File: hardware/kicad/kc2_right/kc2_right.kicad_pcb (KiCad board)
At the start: 2 copper layers, 193.3 x 132.2 mm, 102 parts, among them SW1 KEY_01, SW10 KEY_10, SW11 KEY_11, SW12 KEY_12, SW13 KEY_13, SW14 KEY_14, SW15 KEY_15, SW16 KEY_16, SW17 KEY_17, SW18 KEY_18, SW19 KEY_19, SW2 KEY_02, SW20 KEY_20, SW21 KEY_21, SW22 KEY_22, SW23 KEY_23, SW24 KEY_24, SW25 KEY_25, SW26 KEY_26, SW27 KEY_27, SW28 KEY_28, SW29 KEY_29, SW3 KEY_03, SW30 KEY_30, SW31 KEY_31, SW32 KEY_32, SW33 KEY_33, SW34 KEY_34, SW35 KEY_35, SW36 KEY_36, SW37 KEY_37, SW38 KEY_38, SW39 KEY_39, SW4 KEY_04, SW40 KEY_40, SW41 KEY_41, SW42 KEY_42, SW43 KEY_43, SW44 KEY_44, SW45 KEY_45, SW5 KEY_05, SW6 KEY_06, SW7 KEY_07, SW8 KEY_08, SW9 KEY_09, U1 nice!nano_v2_socket_24pin

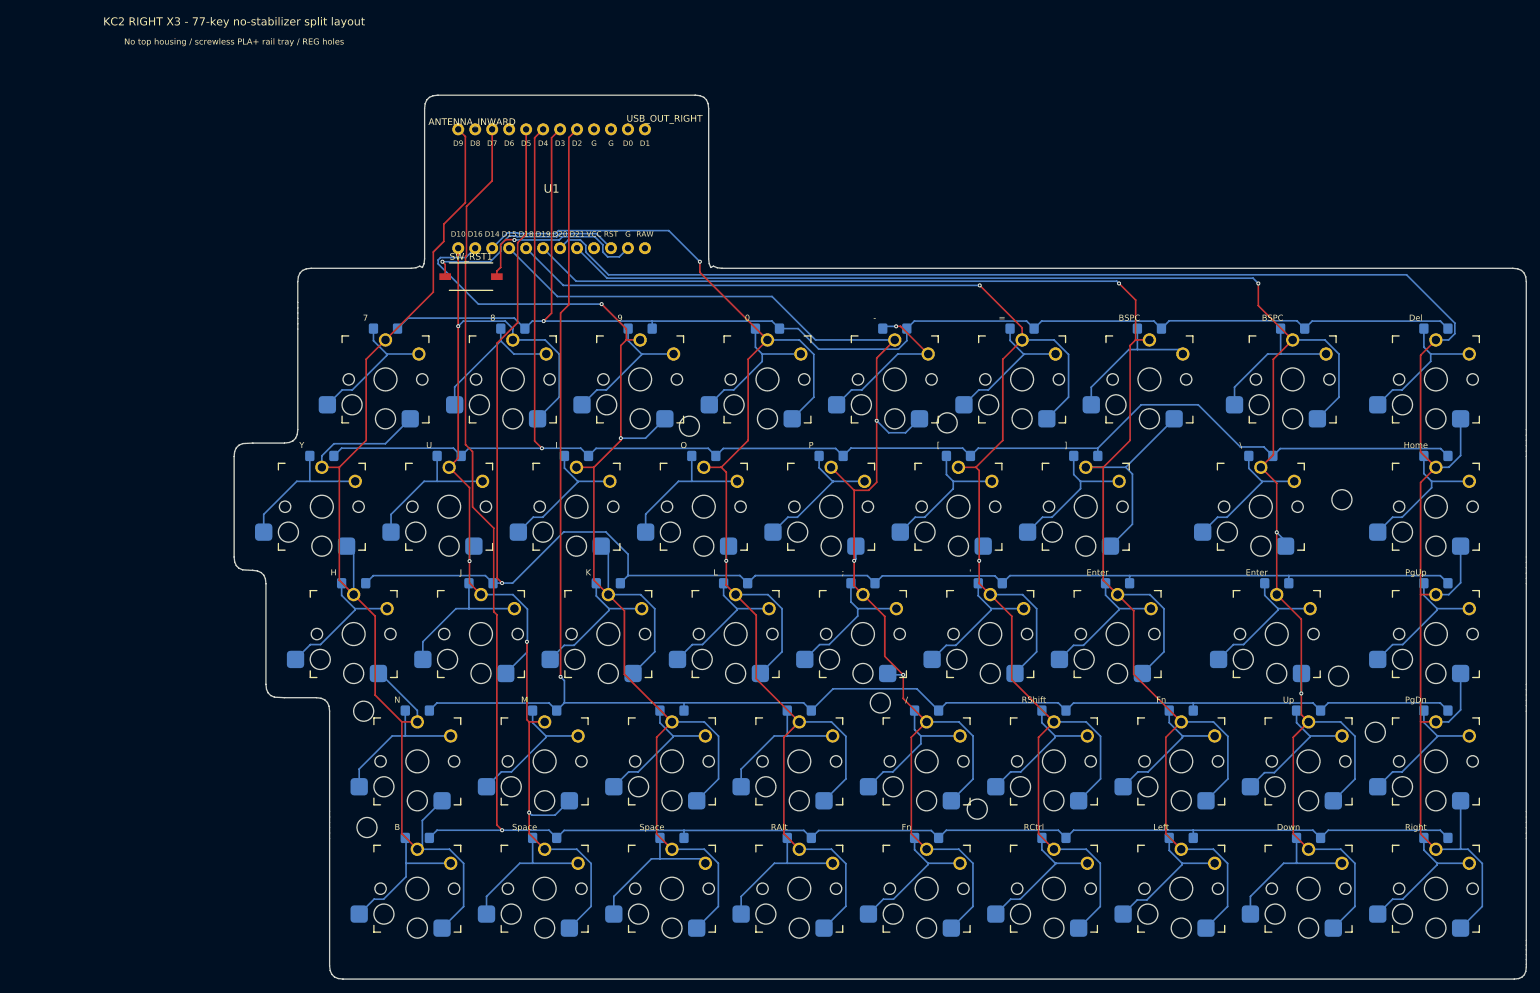
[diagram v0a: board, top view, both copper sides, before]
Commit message: feat(x3-v2): promote active hardware to canonical paths
Align PCB, housing, fabrication artifacts, firmware metadata, tooling, and SRS evidence with OPS-ARCH-006.

Keep fabrication blocked until physical evidence is complete.
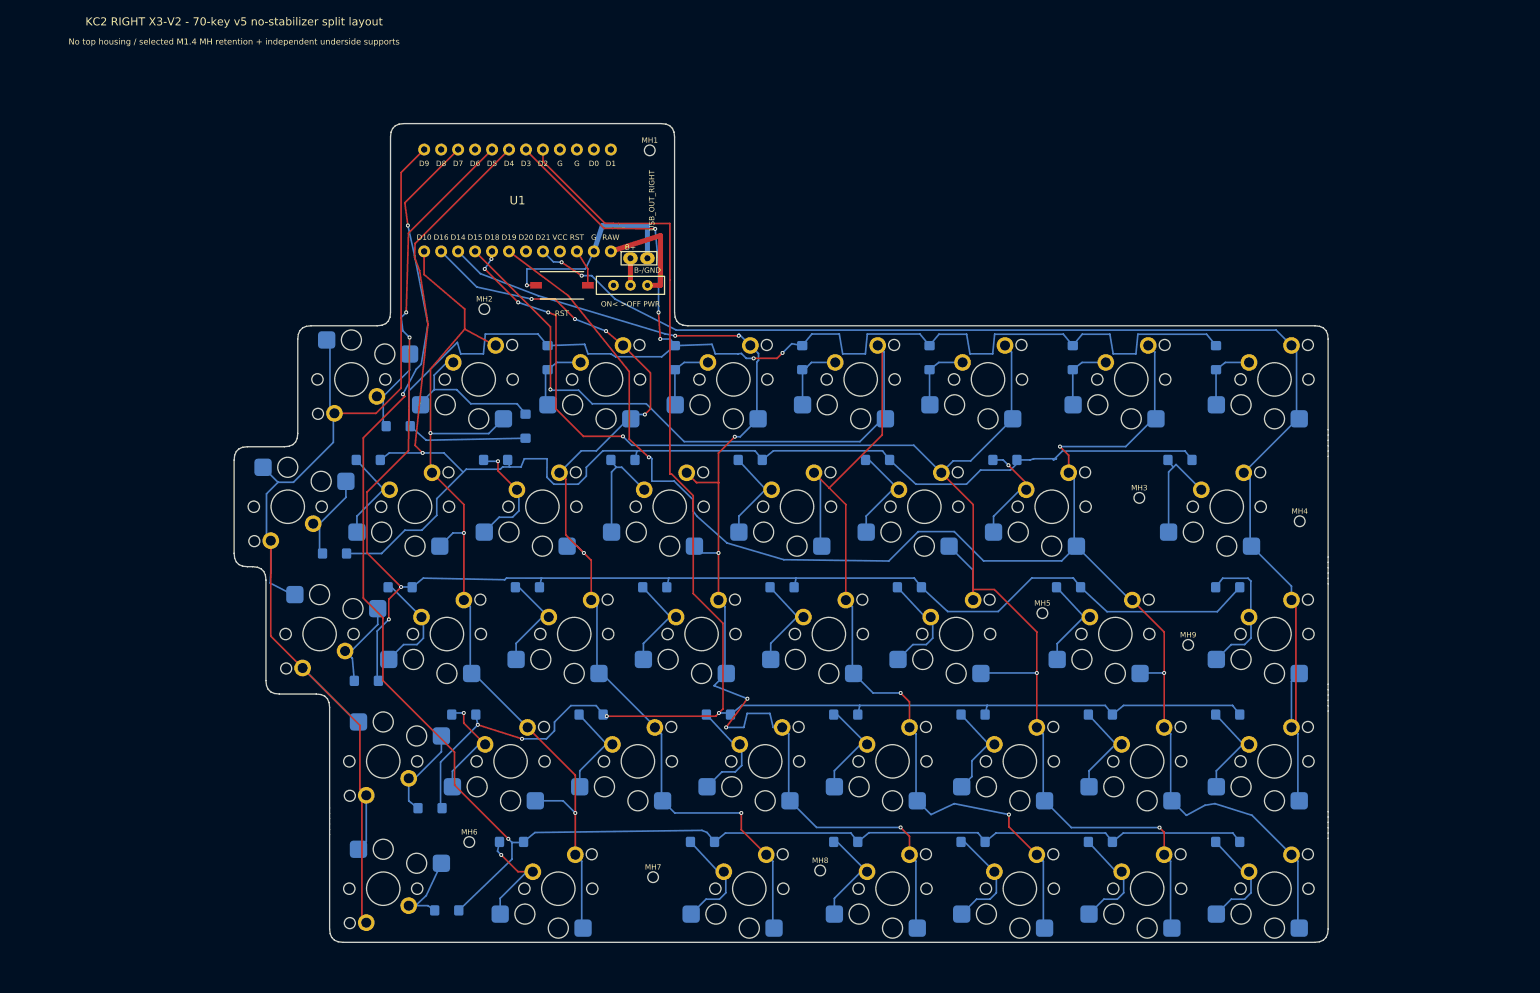
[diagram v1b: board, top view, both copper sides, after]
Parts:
- removed D40, D41, D42, D43, D44, D45: 1N4148W_SOD123_DeviceMart_14592018, D_SOD123_HandSolder_14592018
- removed REG1, REG2, REG3, REG4, REG5, REG6, REG7, REG8, REG9: REG_NPTH_3.0, REG_NPTH_3.0
- removed SW40: KEY_40, SW_Kailh_Choc_V1_HotSwap_THT
- removed SW41: KEY_41, SW_Kailh_Choc_V1_HotSwap_THT
- removed SW42: KEY_42, SW_Kailh_Choc_V1_HotSwap_THT
- removed SW43: KEY_43, SW_Kailh_Choc_V1_HotSwap_THT
- removed SW44: KEY_44, SW_Kailh_Choc_V1_HotSwap_THT
- removed SW45: KEY_45, SW_Kailh_Choc_V1_HotSwap_THT
- added BAT1: 301230_3.7V_100mAh, BAT_301230_30x12mm, F.Cu at (78.4, 50.8)
- added J_BAT1: 301230_DIRECT_SOLDER, BAT_2Pin_PTH_DirectSolder, F.Cu at (94.3, 59.4)
- added MH1: M1.4_NPTH_1.60, MH_M1.4_NPTH_1.60, F.Cu at (97.2, 43.2)
- added MH2: M1.4_NPTH_1.60, MH_M1.4_NPTH_1.60, F.Cu at (72.4, 67.0)
- added MH3: M1.4_NPTH_1.60, MH_M1.4_NPTH_1.60, F.Cu at (170.4, 95.2)
- added MH4: M1.4_NPTH_1.60, MH_M1.4_NPTH_1.60, F.Cu at (194.4, 98.8)
- added MH5: M1.4_NPTH_1.60, MH_M1.4_NPTH_1.60, F.Cu at (155.9, 112.5)
- added MH6: M1.4_NPTH_1.60, MH_M1.4_NPTH_1.60, F.Cu at (70.2, 146.8)
- added MH7: M1.4_NPTH_1.60, MH_M1.4_NPTH_1.60, F.Cu at (97.7, 152.0)
- added MH8: M1.4_NPTH_1.60, MH_M1.4_NPTH_1.60, F.Cu at (122.7, 151.0)
- added MH9: M1.4_NPTH_1.60, MH_M1.4_NPTH_1.60, F.Cu at (177.8, 117.2)
- added SW_PWR1: IMMS-12V_BSI-10, SW_IMMS_12V_BSI10_THT, F.Cu at (94.3, 63.5)
- D1, D10, D11, D12, D13, D14, D15, D16, D17, D18, D19, D2, D20, D21, D22, D23, D24, D25, D26, D27, D28, D29, D3, D30, D31, D32, D33, D34, D35, D36, D37, D38, D39, D4, D5, D6, D7, D8, D9: value 1N4148W_SOD123_DeviceMart_14592018 -> 1N4148W-13-F_DiodesInc_SOD123; footprint D_SOD123_HandSolder_14592018 -> D_1N4148W_SOD123_HandSolder_DiodesInc
- SW1, SW10, SW11, SW12, SW13, SW14, SW15, SW16, SW17, SW18, SW19, SW2, SW20, SW21, SW22, SW23, SW24, SW25, SW26, SW27, SW28, SW29, SW3, SW30, SW31, SW32, SW33, SW34, SW35, SW36, SW37, SW38, SW39, SW4, SW5, SW6, SW7, SW8, SW9: footprint SW_Kailh_Choc_V1_HotSwap_THT -> SW_Choc_V2_Socket_MX_THT
- moved SW9 172.8 mm to (43.0, 96.6), turned to 180 degrees
- moved D9 168.2 mm to (50.0, 103.6)
- moved D18 156.2 mm to (59.8, 108.6)
- moved SW18 149.2 mm to (66.8, 115.6)
- moved SW17 142.1 mm to (47.8, 115.6), turned to 180 degrees
- moved D17 138.0 mm to (54.8, 122.6)
- moved D27 127.9 mm to (88.4, 127.7)
- moved D26 123.2 mm to (69.4, 127.7)
- moved SW27 120.9 mm to (95.4, 134.7)
- moved SW26 116.2 mm to (76.4, 134.7)
- moved SW25 111.5 mm to (57.3, 134.7), turned to 180 degrees
- moved D25 108.2 mm to (64.3, 141.7)
- moved SW33 102.1 mm to (57.3, 153.7), turned to 180 degrees
- moved D34 102.1 mm to (76.5, 146.7)
- moved D33 95.6 mm to (66.8, 157.0)
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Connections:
- D17 pad 1: R_ROW1 -> R_ROW2
- D18 pad 1: R_ROW1 -> R_ROW2
- D25 pad 1: R_ROW2 -> R_ROW3
- D26 pad 1: R_ROW2 -> R_ROW3
- D27 pad 1: R_ROW2 -> R_ROW3
- D33 pad 1: R_ROW3 -> R_ROW4
- D34 pad 1: R_ROW3 -> R_ROW4
- D35 pad 1: R_ROW3 -> R_ROW4
- D36 pad 1: R_ROW3 -> R_ROW4
- D9 pad 1: R_ROW0 -> R_ROW1
- SW10 pad 1: R_COL0 -> R_COL1
- SW11 pad 1: R_COL1 -> R_COL2
- SW12 pad 1: R_COL2 -> R_COL3
- SW13 pad 1: R_COL3 -> R_COL4
- SW14 pad 1: R_COL4 -> R_COL5
- SW15 pad 1: R_COL5 -> R_COL6
- SW16 pad 1: R_COL6 -> R_COL7
- SW17 pad 1: R_COL7 -> R_COL0
- SW18 pad 1: R_COL8 -> R_COL1
- SW19 pad 1: R_COL0 -> R_COL2
- SW20 pad 1: R_COL1 -> R_COL3
- SW21 pad 1: R_COL2 -> R_COL4
- SW22 pad 1: R_COL3 -> R_COL5
- SW23 pad 1: R_COL4 -> R_COL6
- SW24 pad 1: R_COL5 -> R_COL7
- SW25 pad 1: R_COL6 -> R_COL0
- SW26 pad 1: R_COL7 -> R_COL1
- SW27 pad 1: R_COL8 -> R_COL2
- SW28 pad 1: R_COL0 -> R_COL3
- SW29 pad 1: R_COL1 -> R_COL4
- SW30 pad 1: R_COL2 -> R_COL5
- SW31 pad 1: R_COL3 -> R_COL6
- SW32 pad 1: R_COL4 -> R_COL7
- SW33 pad 1: R_COL5 -> R_COL0
- SW34 pad 1: R_COL6 -> R_COL1
- SW35 pad 1: R_COL7 -> R_COL2
- SW36 pad 1: R_COL8 -> R_COL3
- SW37 pad 1: R_COL0 -> R_COL4
- SW38 pad 1: R_COL1 -> R_COL5
- SW39 pad 1: R_COL2 -> R_COL6
- SW9 pad 1: R_COL8 -> R_COL0
- U1 pad RAW: (no net) -> NN_B+
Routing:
- net R_COL8: track 285.3 -> 0.00 mm
- net R_COL7: track 259.8 -> 201.4 mm, vias 3 -> 2
- net R_COL2: track 202.4 -> 151.2 mm, vias 2 -> 6
- net R_COL3: track 216.2 -> 180.9 mm, vias 2 -> 7
- net R_COL6: track 273.8 -> 241.4 mm, vias 1 -> 3
- net RST: track 31.2 -> 5.55 mm, vias 1 -> 0
- net RK40_D: track 22.2 -> 0.00 mm
- net RK44_D: track 22.2 -> 0.00 mm
- net R_ROW0: track 197.6 -> 219.7 mm, vias 1 -> 5
- net R_COL1: track 165.6 -> 143.9 mm, vias 4 -> 3
- net RK45_D: track 21.6 -> 0.00 mm
- net RK41_D: track 21.6 -> 0.00 mm
- net RK43_D: track 21.6 -> 0.00 mm
- net RK42_D: track 21.6 -> 0.00 mm
- net R_ROW4: track 269.1 -> 248.8 mm, vias 1 -> 3
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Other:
- board size 193.3 x 132.2 mm -> 163.7 x 122.5 mm
- board text added: "BAT STRAIN RELIEF"
- board text added: "Diode: Diodes Inc 1N4148W-13-F SOD-123; pad 1 = row cathode"
- board text added: "KC2 RIGHT X3-V2 - 70-key v5 no-stabilizer split layout"
- board text added: "KC2 X3 V2 R"
- board text added: "No top housing / selected M1.4 MH retention + independent underside supports"
- board text added: "ON< >OFF PWR"
- board text added: "RST"
- board text added: "X3 V2: Choc V2 socket OR rotated MX 5-pin direct solder; Choc V1 unsupported"
- board text removed: "BAT LEAD EXIT"
- board text removed: "Battery solders directly to nice!nano B+/B-; no carrier power pads"
- board text removed: "Diode fallback: 1N4148W SOD-123 because DO-35 conflicts with compact hybrid footprint"
- board text removed: "H1"
- board text removed: "H2"
- board text removed: "H3"
- board text removed: "H4"
- board text removed: "H5"
- board text removed: "H6"
- board text removed: "H7"
- board text removed: "H8"
- board text removed: "H9"
- board text removed: "Home"
- board text removed: "KC2 RIGHT X3 - 77-key no-stabilizer split layout"
- board text removed: "KC2 v1.0 R"
- board text removed: "No top housing / screwless PLA+ rail tray / REG holes"
- board text removed: "PgDn"
- board text removed: "PgUp"
- board text removed: "TW301525 80mAh"
- board text removed: "X3: X2 electrical stack, no-stabilizer 77-key split layout"

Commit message: feat(kc2): add solid-floor housing and publish reviewed order guide
CON-ARCH-004/006, OPS-ARCH-007: retain enlarged solder lands and reviewed PCB release; add continuous floors, silicone-foot layouts, CAD/native regression evidence, exact order.md paths, and raw-byte-safe release publication.
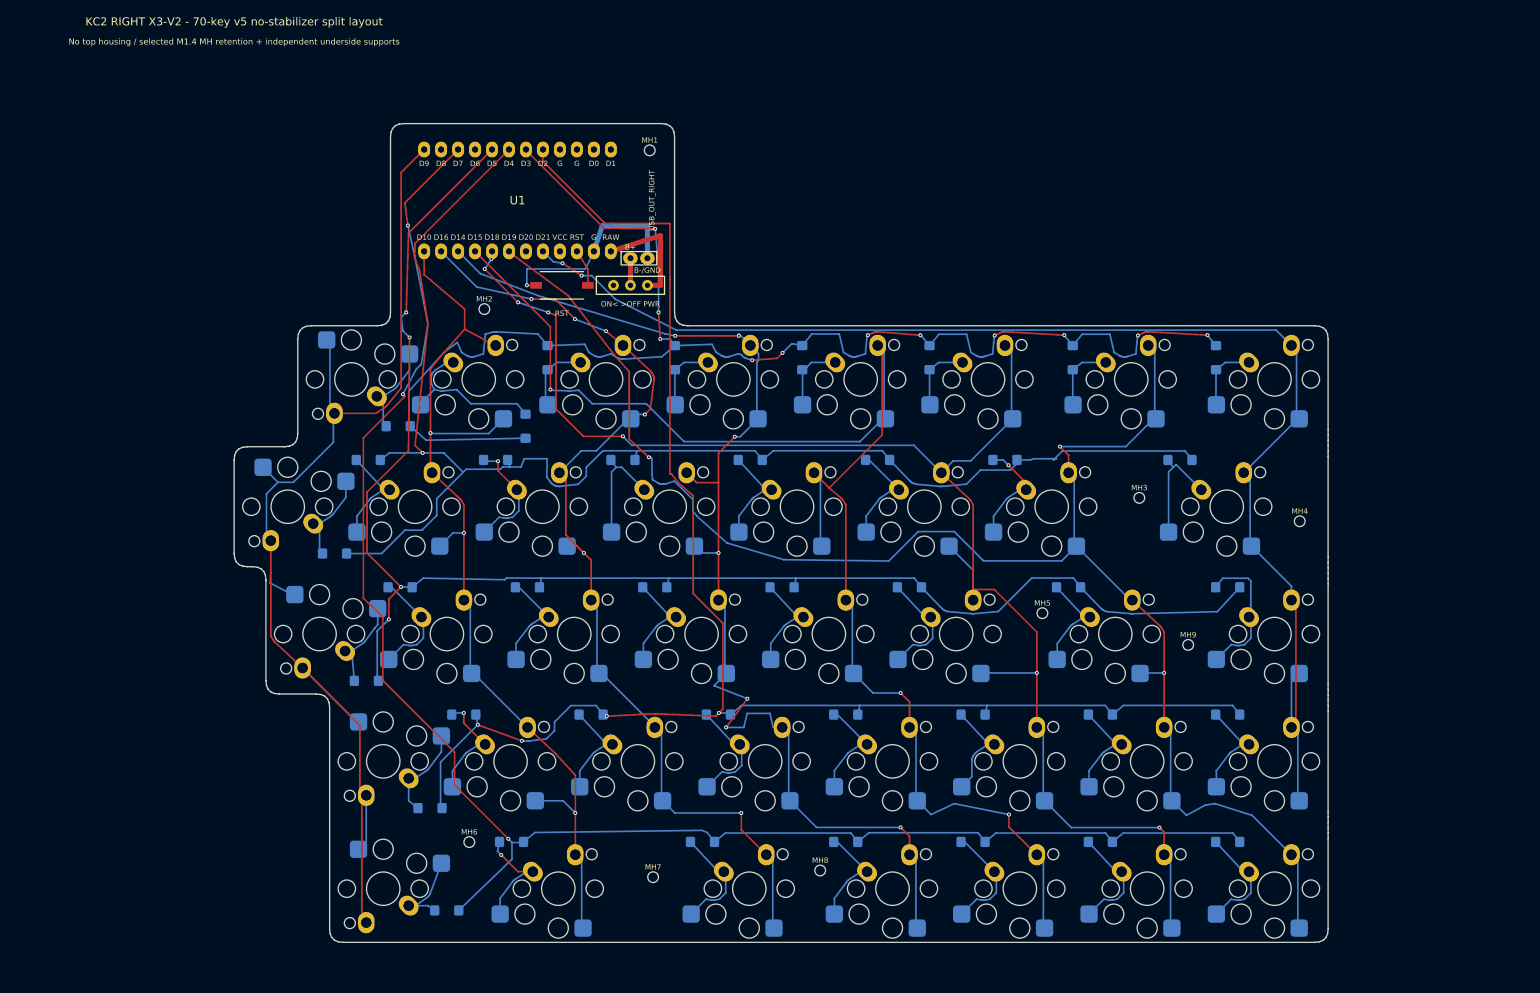
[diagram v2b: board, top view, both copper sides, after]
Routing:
- net R_ROW0: track 219.7 -> 221.3 mm, vias 5 -> 11
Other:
- board text added: "X3 V2: Choc V1+ring / V2 socket OR MX direct solder / receptacles+plate; contact qualification pending"
- board text removed: "X3 V2: Choc V2 socket OR rotated MX 5-pin direct solder; Choc V1 unsupported"
